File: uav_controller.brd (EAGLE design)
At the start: 100 x 80 mm, 22 parts, among them U3 LCD-16X28X2

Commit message: Adding ICSP
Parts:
- added R2, R3: (no value), SparkFun-Resistors:AXIAL-0.3-KIT
- added U$1: PIC-ICSPPOLAR_LOCK, SparkFun-Connectors:MOLEX-1X6_LOCK
- moved R1 8.03 mm to (35.6, 57.1)
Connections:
- removed net N$1: FLIGHTCTRL.2, R1.P$1
- new net MCLR: FLIGHTCTRL.2, R1.P$1, U$1.6
- new net PGC: FLIGHTCTRL.43, R3.P$1, U$1.2
- new net PGD: FLIGHTCTRL.44, R2.P$1, U$1.3
- new net VCC_NC: U$1.5
- net GND: now also U$1.4
- net RWD3: now also R3.P$2; no longer FLIGHTCTRL.43
- net RWD4: now also R2.P$2; no longer FLIGHTCTRL.44
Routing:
- net GND: track 305.9 -> 366.6 mm
- net PGC: track 0.00 -> 34.7 mm
- net PGD: track 0.00 -> 28.8 mm
- net MCLR: track 0.00 -> 23.6 mm
- net 3.3V: track 218.1 -> 209.4 mm
- net N$1: track 6.35 -> 0.00 mm
- net RWD3: track 25.1 -> 28.6 mm
- net RWD4: track 22.6 -> 25.6 mm
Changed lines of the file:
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@@
 <element name="JP4" library="SparkFun-Passives" package="1X02" value="" x="67.31" y="53.34" rot="R270"/>
 <element name="PWRIN" library="SparkFun-Passives" package="1X02" value="" x="67.31" y="67.31" rot="R270"/>
-<element name="R1" library="SparkFun-Resistors" package="AXIAL-0.3EZ" value="" x="33.02" y="49.53" rot="R90"/>
+<element name="R1" library="SparkFun-Resistors" package="AXIAL-0.3EZ" value="" x="35.56" y="57.15" rot="R90"/>
 <element name="HBRIDGE-FRONT" library="SparkFun-PowerIC" package="MULTIWATT15" value="L298" x="58.42" y="30.48" rot="R270"/>
 <element name="HBRIDGE-REAR" library="SparkFun-PowerIC" package="MULTIWATT15" value="L298" x="50.8" y="52.07" rot="R270"/>
@@
 <attribute name="PROD_ID" value="CONN-10681" x="82.55" y="8.89" size="1.778" layer="27" rot="R270" display="off"/>
 </element>
+<element name="U$1" library="SparkFun-Connectors" package="MOLEX-1X6_LOCK" value="PIC-ICSPPOLAR_LOCK" x="15.24" y="55.88"/>
+<element name="R2" library="SparkFun-Resistors" package="AXIAL-0.3-KIT" value="" x="24.13" y="46.99"/>
+<element name="R3" library="SparkFun-Resistors" package="AXIAL-0.3-KIT" value="" x="21.59" y="50.8"/>
 </elements>
 <signals>
@@
 <wire x1="77.47" y1="2.54" x2="77.47" y2="10.16" width="0.4064" layer="16"/>
 <wire x1="77.47" y1="10.16" x2="80.01" y2="10.16" width="0.4064" layer="16"/>
-<wire x1="61.11" y1="30.54" x2="62.29" y2="52.13" width="0" layer="19" extent="1-1"/>
-<wire x1="7.54" y1="66.04" x2="7.54" y2="57.15" width="0" layer="19" extent="1-1"/>
+<contactref element="U$1" pad="4"/>
+<wire x1="22.86" y1="55.626" x2="22.86" y2="55.88" width="0.4064" layer="1"/>
+<wire x1="22.86" y1="55.88" x2="21.59" y2="57.15" width="0.4064" layer="1"/>
+<wire x1="21.59" y1="57.15" x2="7.54" y2="57.15" width="0.4064" layer="1"/>
+<wire x1="39.37" y1="68.58" x2="30.48" y2="68.58" width="0.4064" layer="16"/>
+<wire x1="30.48" y1="68.58" x2="26.67" y2="64.77" width="0.4064" layer="16"/>
+<wire x1="26.67" y1="64.77" x2="22.86" y2="60.96" width="0.4064" layer="16"/>
+<wire x1="22.86" y1="60.96" x2="22.86" y2="55.626" width="0.4064" layer="16"/>
+<wire x1="8.89" y1="64.77" x2="7.62" y2="66.04" width="0.254" layer="16"/>
+<wire x1="26.67" y1="64.77" x2="8.89" y2="64.77" width="0.254" layer="16"/>
+<wire x1="7.62" y1="66.04" x2="7.54" y2="66.04" width="0.254" layer="16"/>
 </signal>
 <signal name="3.3V">
@@
 <wire x1="50.8" y1="63.5" x2="50.8" y2="53.25" width="0.4064" layer="16"/>
 <wire x1="50.8" y1="53.25" x2="48.41" y2="50.86" width="0.4064" layer="16"/>
-<wire x1="48.41" y1="50.86" x2="35.5" y2="50.86" width="0.4064" layer="1"/>
-<wire x1="35.5" y1="50.86" x2="33.02" y2="53.34" width="0.4064" layer="1"/>
 <contactref element="L3G4200D" pad="7"/>
 <wire x1="7.493" y1="34.29" x2="22.86" y2="34.29" width="0.4064" layer="1"/>
@@
 <wire x1="26.67" y1="33.02" x2="27.94" y2="31.75" width="0.4064" layer="1"/>
 <contactref element="RANGE_VOLTAGE" pad="1"/>
-<wire x1="33.02" y1="53.34" x2="30.48" y2="55.88" width="0.4064" layer="1"/>
-<wire x1="30.48" y1="55.88" x2="30.48" y2="62.23" width="0.4064" layer="1"/>
-<wire x1="30.48" y1="62.23" x2="27.94" y2="62.23" width="0.4064" layer="1"/>
-<wire x1="27.94" y1="62.23" x2="26.67" y2="60.96" width="0.4064" layer="1"/>
 <contactref element="JP7" pad="1"/>
 <contactref element="JP5" pad="1"/>
@@
 <wire x1="83.82" y1="33.02" x2="85.09" y2="31.75" width="0.4064" layer="1"/>
 <wire x1="85.09" y1="31.75" x2="85.09" y2="30.48" width="0.4064" layer="1"/>
+<wire x1="35.56" y1="60.96" x2="33.02" y2="63.5" width="0.4064" layer="16"/>
+<wire x1="33.02" y1="63.5" x2="29.21" y2="63.5" width="0.4064" layer="16"/>
+<wire x1="29.21" y1="63.5" x2="26.67" y2="60.96" width="0.4064" layer="16"/>
+<wire x1="44.45" y1="66.04" x2="43.18" y2="66.04" width="0.4064" layer="16"/>
+<wire x1="43.18" y1="66.04" x2="40.64" y2="63.5" width="0.4064" layer="16"/>
+<wire x1="40.64" y1="63.5" x2="38.1" y2="63.5" width="0.4064" layer="16"/>
+<wire x1="38.1" y1="63.5" x2="35.56" y2="60.96" width="0.4064" layer="16"/>
 </signal>
 <signal name="VCC">
@@
 </signal>
 <signal name="RWD3">
-<contactref element="FLIGHTCTRL" pad="43"/>
 <contactref element="HBRIDGE-REAR" pad="10"/>
-<wire x1="38.1" y1="36.83" x2="39.37" y2="38.1" width="0.4064" layer="16"/>
-<wire x1="39.37" y1="38.1" x2="39.37" y2="45.72" width="0.4064" layer="16"/>
-<wire x1="39.37" y1="45.72" x2="43.18" y2="49.53" width="0.4064" layer="16"/>
-<wire x1="43.18" y1="49.53" x2="53.43" y2="49.53" width="0.4064" layer="16"/>
-<wire x1="53.43" y1="49.53" x2="53.49" y2="49.59" width="0.4064" layer="16"/>
+<contactref element="R3" pad="P$2"/>
+<wire x1="53.49" y1="49.59" x2="26.61" y2="49.59" width="0.4064" layer="1"/>
+<wire x1="26.61" y1="49.59" x2="25.4" y2="50.8" width="0.4064" layer="1"/>
 </signal>
 <signal name="RWD4">
-<contactref element="FLIGHTCTRL" pad="44"/>
 <contactref element="HBRIDGE-REAR" pad="12"/>
-<wire x1="35.56" y1="39.37" x2="35.56" y2="41.91" width="0.4064" layer="1"/>
-<wire x1="35.56" y1="41.91" x2="40.64" y2="46.99" width="0.4064" layer="1"/>
-<wire x1="40.64" y1="46.99" x2="53.43" y2="46.99" width="0.4064" layer="1"/>
-<wire x1="53.43" y1="46.99" x2="53.49" y2="47.05" width="0.4064" layer="1"/>
-</signal>
-<signal name="N$1">
+<contactref element="R2" pad="P$2"/>
+<wire x1="53.49" y1="47.05" x2="28" y2="47.05" width="0.4064" layer="1"/>
+<wire x1="28" y1="47.05" x2="27.94" y2="46.99" width="0.4064" layer="1"/>
+</signal>
+<signal name="MCLR">
 <contactref element="FLIGHTCTRL" pad="2"/>
 <contactref element="R1" pad="P$1"/>
+<contactref element="U$1" pad="6"/>
+<wire x1="35.56" y1="53.34" x2="30.226" y2="53.34" width="0.4064" layer="1"/>
+<wire x1="30.226" y1="53.34" x2="27.94" y2="55.626" width="0.4064" layer="1"/>
+<wire x1="35.56" y1="53.34" x2="35.56" y2="48.26" width="0.4064" layer="16"/>
+<wire x1="35.56" y1="48.26" x2="33.02" y2="45.72" width="0.4064" layer="16"/>
 <wire x1="33.02" y1="45.72" x2="33.02" y2="39.37" width="0.4064" layer="16"/>
 </signal>
@@
 <wire x1="81.28" y1="26.67" x2="81.28" y2="17.78" width="0.4064" layer="16"/>
 </signal>
+<signal name="VCC_NC">
+<contactref element="U$1" pad="5"/>
+</signal>
+<signal name="PGD">
+<contactref element="U$1" pad="3"/>
+<contactref element="FLIGHTCTRL" pad="44"/>
+<contactref element="R2" pad="P$1"/>
+<wire x1="20.32" y1="55.88" x2="20.32" y2="46.99" width="0.4064" layer="1"/>
+<wire x1="35.56" y1="39.37" x2="35.56" y2="41.91" width="0.4064" layer="1"/>
+<wire x1="35.56" y1="41.91" x2="25.4" y2="41.91" width="0.4064" layer="1"/>
+<wire x1="25.4" y1="41.91" x2="20.32" y2="46.99" width="0.4064" layer="1"/>
+</signal>
+<signal name="PGC">
+<contactref element="U$1" pad="2"/>
+<contactref element="FLIGHTCTRL" pad="43"/>
+<contactref element="R3" pad="P$1"/>
+<wire x1="17.78" y1="55.626" x2="17.78" y2="50.8" width="0.4064" layer="1"/>
+<wire x1="38.1" y1="36.83" x2="36.83" y2="38.1" width="0.4064" layer="1"/>
+<wire x1="36.83" y1="38.1" x2="34.29" y2="38.1" width="0.4064" layer="1"/>
+<wire x1="34.29" y1="38.1" x2="34.29" y2="40.64" width="0.4064" layer="1"/>
+<wire x1="34.29" y1="40.64" x2="24.13" y2="40.64" width="0.4064" layer="1"/>
+<wire x1="24.13" y1="40.64" x2="17.78" y2="46.99" width="0.4064" layer="1"/>
+<wire x1="17.78" y1="46.99" x2="17.78" y2="50.8" width="0.4064" layer="1"/>
+</signal>
 </signals>

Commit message: Metadata changed I guess?
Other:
- board size 100 x 80 mm -> 91.1 x 74.9 mm
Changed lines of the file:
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@@
 <board>
 <plain>
-<wire x1="0" y1="0" x2="100" y2="0" width="0" layer="20"/>
-<wire x1="100" y1="0" x2="100" y2="80" width="0" layer="20"/>
-<wire x1="100" y1="80" x2="0" y2="80" width="0" layer="20"/>
-<wire x1="0" y1="80" x2="0" y2="0" width="0" layer="20"/>
+<wire x1="0" y1="0" x2="91.11" y2="0" width="0" layer="20"/>
+<wire x1="91.11" y1="0" x2="91.11" y2="74.92" width="0" layer="20"/>
+<wire x1="91.11" y1="74.92" x2="0" y2="74.92" width="0" layer="20"/>
+<wire x1="0" y1="74.92" x2="0" y2="0" width="0" layer="20"/>
 </plain>
 <attributes>

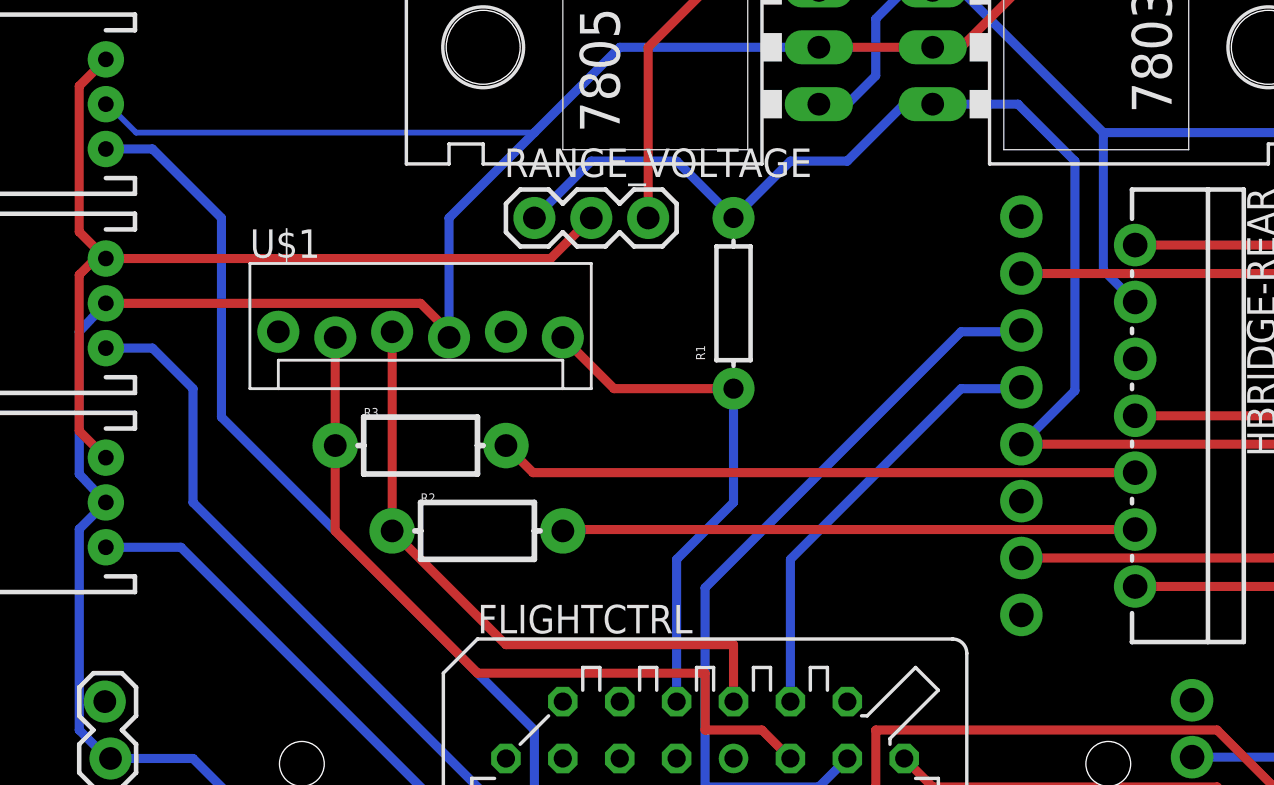
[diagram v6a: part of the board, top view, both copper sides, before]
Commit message: Relabeled parts for clarity
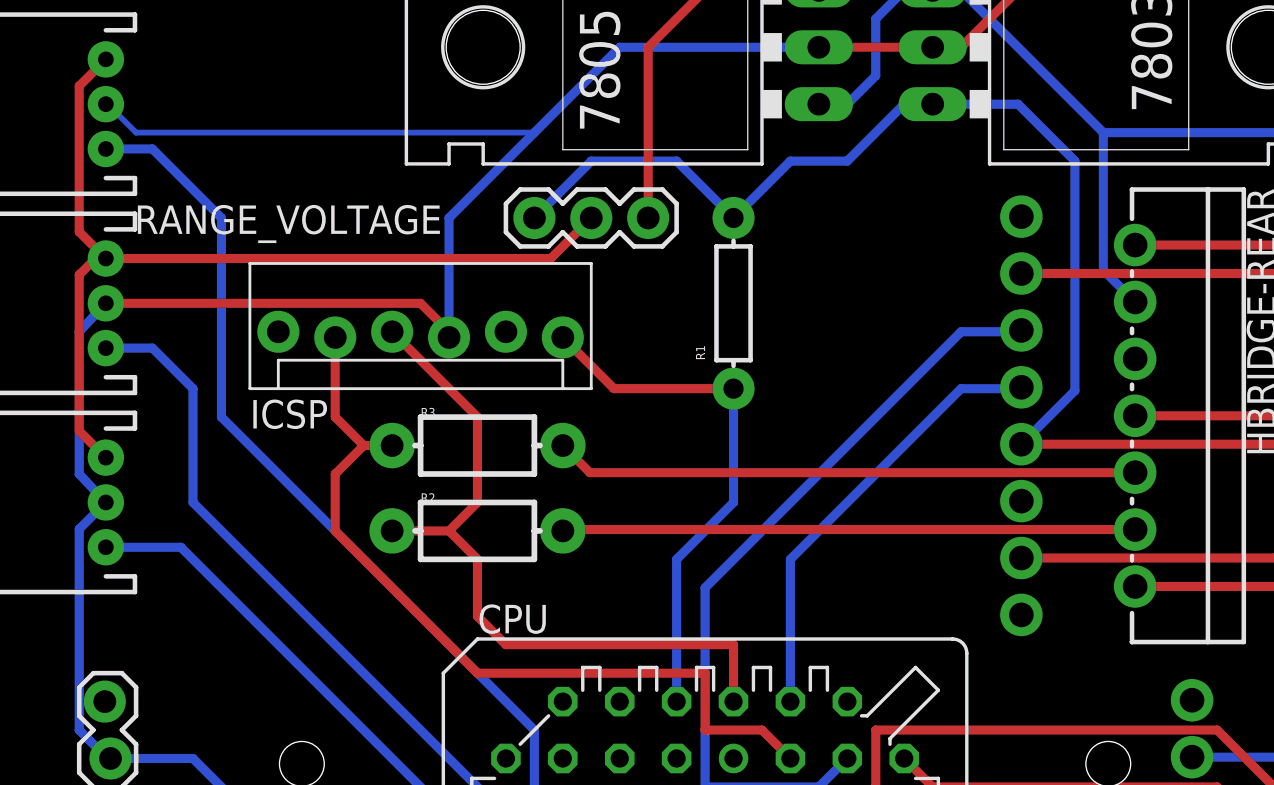
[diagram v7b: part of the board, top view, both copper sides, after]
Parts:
- CPU: value PIC16F877SO -> '16F877
- ICSP: value PIC-ICSPPOLAR_LOCK -> (none)
- moved R3 2.54 mm to (24.1, 50.8)
- renumbered FLIGHTCTRL to CPU, U$1 to ICSP
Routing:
- net PGD: track 28.8 -> 32.4 mm
- net RWD3: track 28.6 -> 26.1 mm
- net PGC: track 34.7 -> 37.0 mm
